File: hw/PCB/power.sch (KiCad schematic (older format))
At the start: 12 parts, among them J4 Battery, U0 AP7215-33YG-13, U3 AV4524

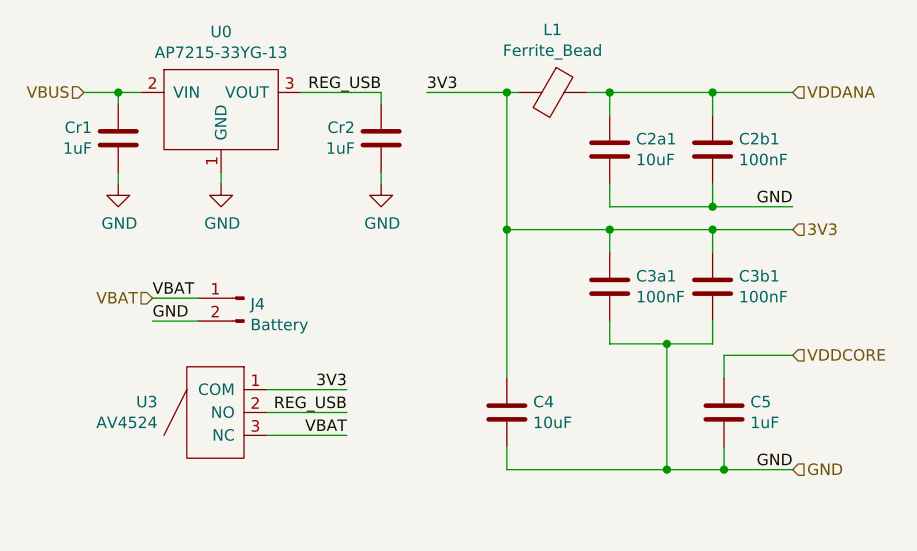
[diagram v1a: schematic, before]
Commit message: Added a footprint library for a micro SD card. Updated the schematic. Replaced the SAMD21G with the SAMD21E (32 pin variant). Added a data logger and a reset button.
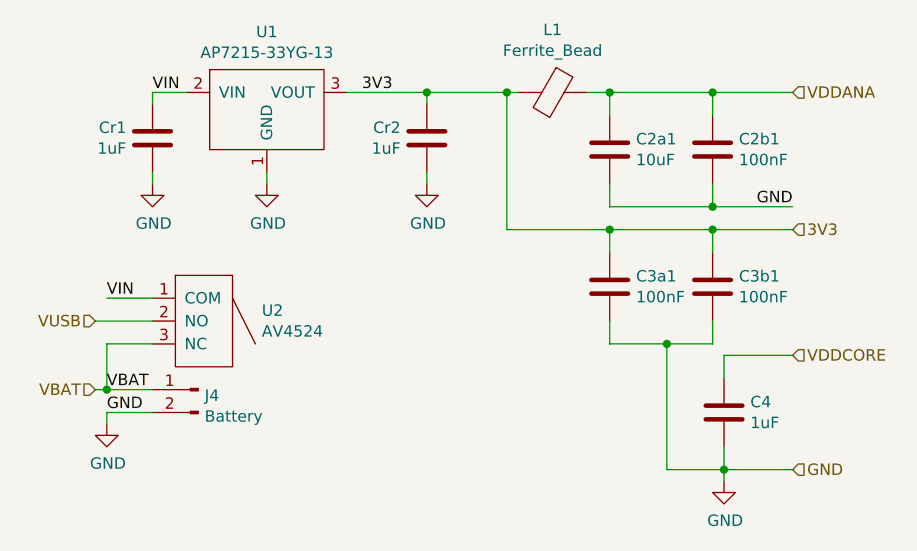
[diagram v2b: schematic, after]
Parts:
- removed C4: 10uF, Capacitor_SMD:C_0603_1608Metric_Pad1.05x0.95mm_HandSolder, symbol Device:C
- removed U3: AV4524, Interrupt:AV4524, symbol Interrupter:AV4524
- added U2: AV4524, Interrupt:AV4524, symbol Interrupter:AV4524
- renumbered C5 to C4, U0 to U1
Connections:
- net REG_USB is gone; now on net 3V3: Cr2.1, U1.3 (VOUT)
- net VBAT: now also U2.3 (NC)
- net VBUS renamed VIN
- net VIN: now also U2.1 (COM)
- new net VUSB: U2.2 (NO)
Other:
- moved on the sheet: Cr1, Cr2, J4, U1
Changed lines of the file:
@@
 $EndComp
 $Comp
-L Device:C C5
+L Device:C C4
 U 1 1 5B635301
 P 5100 4800
-F 0 "C5" H 5215 4846 50  0000 L CNN
+F 0 "C4" H 5215 4846 50  0000 L CNN
 F 1 "1uF" H 5215 4755 50  0000 L CNN
 F 2 "Capacitor_SMD:C_0603_1608Metric_Pad1.05x0.95mm_HandSolder" H 5138 4650 50  0001 C CNN
@@
 $EndComp
 $Comp
-L Device:C C4
-U 1 1 5B635382
-P 4150 4800
-F 0 "C4" H 4265 4846 50  0000 L CNN
-F 1 "10uF" H 4265 4755 50  0000 L CNN
-F 2 "Capacitor_SMD:C_0603_1608Metric_Pad1.05x0.95mm_HandSolder" H 4188 4650 50  0001 C CNN
-F 3 "~" H 4150 4800 50  0001 C CNN
-	1    4150 4800
-	1    0    0    -1
-$EndComp
-$Comp
 L Device:C C3a1
 U 1 1 5B6353CA
@@
 Text HLabel 5400 5050 2    50   Input ~ 0
 GND
-Wire Wire Line
-	4150 4650 4150 4000
-Wire Wire Line
-	4150 4950 4150 5050
-Wire Wire Line
-	4150 5050 4850 5050
 Connection ~ 5100 5050
 Text Label 5400 3900 2    50   ~ 0
 GND
-Text Label 5400 5050 2    50   ~ 0
+Text Label 2400 4800 0    50   ~ 0
 GND
-Connection ~ 4150 4000
 Wire Wire Line
 	4150 4000 4150 3400
@@
 Wire Wire Line
 	4850 4500 4600 4500
-Connection ~ 4850 5050
 Wire Wire Line
 	4850 5050 5100 5050
@@
 Connection ~ 4850 4500
 $Comp
-L power_regul:AP7215-33YG-13 U0
+L power_regul:AP7215-33YG-13 U1
 U 1 1 5BB07412
-P 2900 3550
-F 0 "U0" H 2900 3965 50  0000 C CNN
-F 1 "AP7215-33YG-13" H 2900 3874 50  0000 C CNN
-F 2 "Package_TO_SOT_SMD:SOT-89-3_Handsoldering" H 2900 3550 50  0001 C CNN
-F 3 "" H 2900 3550 50  0001 C CNN
-	1    2900 3550
+P 3100 3550
+F 0 "U1" H 3100 3965 50  0000 C CNN
+F 1 "AP7215-33YG-13" H 3100 3874 50  0000 C CNN
+F 2 "Package_TO_SOT_SMD:SOT-89-3_Handsoldering" H 3100 3550 50  0001 C CNN
+F 3 "" H 3100 3550 50  0001 C CNN
+	1    3100 3550
 	1    0    0    -1
 $EndComp
@@
 	5400 4000 5050 4000
 Connection ~ 5050 4000
-Text HLabel 2300 3400 0    50   Input ~ 0
-VBUS
 $Comp
 L Device:C Cr1
 U 1 1 5BB30701
-P 2450 3600
-F 0 "Cr1" H 2565 3646 50  0000 L CNN
-F 1 "1uF" H 2565 3555 50  0000 L CNN
-F 2 "Capacitor_SMD:C_0603_1608Metric_Pad1.05x0.95mm_HandSolder" H 2488 3450 50  0001 C CNN
-F 3 "~" H 2450 3600 50  0001 C CNN
-	1    2450 3600
+P 2600 3600
+F 0 "Cr1" H 2715 3646 50  0000 L CNN
+F 1 "1uF" H 2715 3555 50  0000 L CNN
+F 2 "Capacitor_SMD:C_0603_1608Metric_Pad1.05x0.95mm_HandSolder" H 2638 3450 50  0001 C CNN
+F 3 "~" H 2600 3600 50  0001 C CNN
+	1    2600 3600
 	-1   0    0    -1
 $EndComp
@@
 L Device:C Cr2
 U 1 1 5BB3073D
-P 3600 3600
-F 0 "Cr2" H 3715 3646 50  0000 L CNN
-F 1 "1uF" H 3715 3555 50  0000 L CNN
-F 2 "Capacitor_SMD:C_0603_1608Metric_Pad1.05x0.95mm_HandSolder" H 3638 3450 50  0001 C CNN
-F 3 "~" H 3600 3600 50  0001 C CNN
-	1    3600 3600
+P 3800 3600
+F 0 "Cr2" H 3915 3646 50  0000 L CNN
+F 1 "1uF" H 3915 3555 50  0000 L CNN
+F 2 "Capacitor_SMD:C_0603_1608Metric_Pad1.05x0.95mm_HandSolder" H 3838 3450 50  0001 C CNN
+F 3 "~" H 3800 3600 50  0001 C CNN
+	1    3800 3600
 	-1   0    0    -1
 $EndComp
 Connection ~ 4150 3400
 Wire Wire Line
-	2300 3400 2450 3400
-Wire Wire Line
-	2450 3450 2450 3400
-Connection ~ 2450 3400
-Wire Wire Line
-	2450 3400 2550 3400
-Wire Wire Line
-	2450 3750 2450 3800
-Wire Wire Line
-	3600 3750 3600 3800
+	2600 3450 2600 3400
+Wire Wire Line
+	2600 3750 2600 3800
+Wire Wire Line
+	3800 3750 3800 3800
 $Comp
 L power:GND #PWR0107
 U 1 1 5BB332C0
-P 2450 3800
-F 0 "#PWR0107" H 2450 3550 50  0001 C CNN
-F 1 "GND" H 2455 3627 50  0000 C CNN
-F 2 "" H 2450 3800 50  0001 C CNN
-F 3 "" H 2450 3800 50  0001 C CNN
-	1    2450 3800
+P 2600 3800
+F 0 "#PWR0107" H 2600 3550 50  0001 C CNN
+F 1 "GND" H 2605 3627 50  0000 C CNN
+F 2 "" H 2600 3800 50  0001 C CNN
+F 3 "" H 2600 3800 50  0001 C CNN
+	1    2600 3800
 	1    0    0    -1
 $EndComp
@@
 L power:GND #PWR0108
 U 1 1 5BB332E6
-P 3600 3800
-F 0 "#PWR0108" H 3600 3550 50  0001 C CNN
-F 1 "GND" H 3605 3627 50  0000 C CNN
-F 2 "" H 3600 3800 50  0001 C CNN
-F 3 "" H 3600 3800 50  0001 C CNN
-	1    3600 3800
+P 3800 3800
+F 0 "#PWR0108" H 3800 3550 50  0001 C CNN
+F 1 "GND" H 3805 3627 50  0000 C CNN
+F 2 "" H 3800 3800 50  0001 C CNN
+F 3 "" H 3800 3800 50  0001 C CNN
+	1    3800 3800
 	1    0    0    -1
 $EndComp
@@
 L power:GND #PWR0113
 U 1 1 5BF7FABB
-P 2900 3800
-F 0 "#PWR0113" H 2900 3550 50  0001 C CNN
-F 1 "GND" H 2905 3627 50  0000 C CNN
-F 2 "" H 2900 3800 50  0001 C CNN
-F 3 "" H 2900 3800 50  0001 C CNN
-	1    2900 3800
-	1    0    0    -1
-$EndComp
-Wire Wire Line
-	2900 3800 2900 3750
-Text Label 3600 3400 2    50   ~ 0
-REG_USB
-Wire Wire Line
-	3250 3400 3600 3400
-Text Label 3800 3400 0    50   ~ 0
+P 3100 3800
+F 0 "#PWR0113" H 3100 3550 50  0001 C CNN
+F 1 "GND" H 3105 3627 50  0000 C CNN
+F 2 "" H 3100 3800 50  0001 C CNN
+F 3 "" H 3100 3800 50  0001 C CNN
+	1    3100 3800
+	1    0    0    -1
+$EndComp
+Wire Wire Line
+	3100 3800 3100 3750
+Wire Wire Line
+	3450 3400 3800 3400
+Text Label 3650 3400 2    50   ~ 0
 3V3
-Text HLabel 2600 4300 0    50   Input ~ 0
-VBAT
 $Comp
 L Connector:Conn_01x02_Male J4
 U 1 1 5BFD4B3E
-P 3000 4300
-F 0 "J4" H 2972 4274 50  0000 R CNN
-F 1 "Battery" H 2972 4183 50  0000 R CNN
-F 2 "Connector_JST:JST_PH_S2B-PH-K_1x02_P2.00mm_Horizontal" H 3000 4300 50  0001 C CNN
-F 3 "~" H 3000 4300 50  0001 C CNN
-	1    3000 4300
+P 2800 4700
+F 0 "J4" H 2772 4674 50  0000 R CNN
+F 1 "Battery" H 2772 4583 50  0000 R CNN
+F 2 "Connector_JST:JST_PH_S2B-PH-K_1x02_P2.00mm_Horizontal" H 2800 4700 50  0001 C CNN
+F 3 "~" H 2800 4700 50  0001 C CNN
+	1    2800 4700
 	-1   0    0    -1
 $EndComp
-Text Label 2600 4400 0    50   ~ 0
-GND
-Text Label 2600 4300 0    50   ~ 0
+Wire Wire Line
+	3800 3400 4150 3400
+Wire Wire Line
+	3800 3450 3800 3400
+$Comp
+L Interrupter:AV4524 U2
+U 1 1 5D1D3759
+P 2800 4400
+F 0 "U2" H 3078 4446 50  0000 L CNN
+F 1 "AV4524" H 3078 4355 50  0000 L CNN
+F 2 "Interrupt:AV4524" H 2750 4400 50  0001 C CNN
+F 3 "" H 2750 4400 50  0001 C CNN
+	1    2800 4400
+	1    0    0    -1
+$EndComp
+Text HLabel 2350 4700 0    50   Input ~ 0
 VBAT
-Wire Wire Line
-	2800 4300 2600 4300
-Wire Wire Line
-	2600 4400 2800 4400
-Wire Wire Line
-	3800 3400 4150 3400
-Wire Wire Line
-	3600 3450 3600 3400
-$Comp
-L Interrupter:AV4524 U3
-U 1 1 5BFC5BF6
-P 2900 4800
-F 0 "U3" H 3178 4846 50  0000 L CNN
-F 1 "AV4524" H 3178 4755 50  0000 L CNN
-F 2 "Interrupt:AV4524" H 2850 4800 50  0001 C CNN
-F 3 "" H 2850 4800 50  0001 C CNN
-	1    2900 4800
-	-1   0    0    -1
-$EndComp
-Text Label 3450 4700 2    50   ~ 0
-3V3
-Text Label 3450 4900 2    50   ~ 0
+Text HLabel 2350 4400 0    50   Input ~ 0
+VUSB
+Text Label 2400 4300 0    50   ~ 0
+VIN
+Text Label 2400 4700 0    50   ~ 0
 VBAT
-Text Label 3450 4800 2    50   ~ 0
-REG_USB
-Wire Wire Line
-	3450 4800 3100 4800
-Wire Wire Line
-	3100 4900 3450 4900
-Wire Wire Line
-	3100 4700 3450 4700
+Wire Wire Line
+	2600 4400 2350 4400
+Wire Wire Line
+	2600 4500 2400 4500
+Wire Wire Line
+	2600 4300 2400 4300
+Wire Wire Line
+	2400 4500 2400 4700
+Wire Wire Line
+	2400 4700 2600 4700
+$Comp
+L power:GND #PWR?
+U 1 1 5D1DFE0F
+P 2400 4850
+F 0 "#PWR?" H 2400 4600 50  0001 C CNN
+F 1 "GND" H 2405 4677 50  0000 C CNN
+F 2 "" H 2400 4850 50  0001 C CNN
+F 3 "" H 2400 4850 50  0001 C CNN
+	1    2400 4850
+	1    0    0    -1
+$EndComp
+Text Label 2600 3400 0    50   ~ 0
+VIN
+Connection ~ 3800 3400
+Wire Wire Line
+	2400 4800 2600 4800
+Wire Wire Line
+	2400 4850 2400 4800
+$Comp
+L power:GND #PWR?
+U 1 1 5D1EBCCE
+P 5100 5100
+F 0 "#PWR?" H 5100 4850 50  0001 C CNN
+F 1 "GND" H 5105 4927 50  0000 C CNN
+F 2 "" H 5100 5100 50  0001 C CNN
+F 3 "" H 5100 5100 50  0001 C CNN
+	1    5100 5100
+	1    0    0    -1
+$EndComp
+Wire Wire Line
+	5100 5100 5100 5050
+Wire Wire Line
+	2600 3400 2750 3400
+Wire Wire Line
+	2400 4700 2350 4700
+Connection ~ 2400 4700
 $EndSCHEMATC

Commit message: Started the new design of the PCB's layout.
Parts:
- U1: footprint Package_TO_SOT_SMD:SOT-89-3_Handsoldering -> Package_TO_SOT_SMD:SOT-89-3
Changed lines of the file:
@@
 $Descr A4 11693 8268
 encoding utf-8
-Sheet 2 5
+Sheet 2 6
 Title ""
 Date ""
@@
 F 0 "U1" H 3100 3965 50  0000 C CNN
 F 1 "AP7215-33YG-13" H 3100 3874 50  0000 C CNN
-F 2 "Package_TO_SOT_SMD:SOT-89-3_Handsoldering" H 3100 3550 50  0001 C CNN
+F 2 "Package_TO_SOT_SMD:SOT-89-3" H 3100 3550 50  0001 C CNN
 F 3 "" H 3100 3550 50  0001 C CNN
 	1    3100 3550
@@
 	2400 4700 2600 4700
 $Comp
-L power:GND #PWR?
+L power:GND #PWR0115
 U 1 1 5D1DFE0F
 P 2400 4850
-F 0 "#PWR?" H 2400 4600 50  0001 C CNN
+F 0 "#PWR0115" H 2400 4600 50  0001 C CNN
 F 1 "GND" H 2405 4677 50  0000 C CNN
 F 2 "" H 2400 4850 50  0001 C CNN
@@
 	2400 4850 2400 4800
 $Comp
-L power:GND #PWR?
+L power:GND #PWR0116
 U 1 1 5D1EBCCE
 P 5100 5100
-F 0 "#PWR?" H 5100 4850 50  0001 C CNN
+F 0 "#PWR0116" H 5100 4850 50  0001 C CNN
 F 1 "GND" H 5105 4927 50  0000 C CNN
 F 2 "" H 5100 5100 50  0001 C CNN

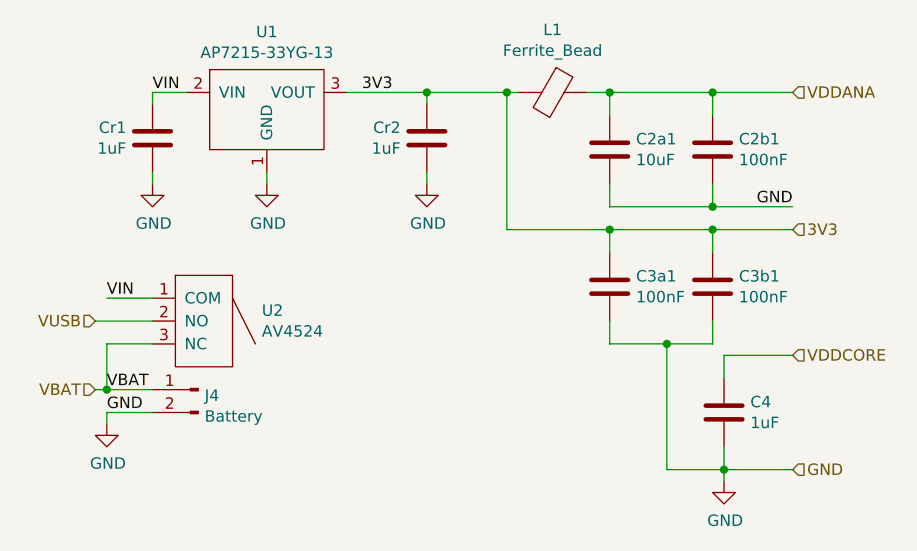
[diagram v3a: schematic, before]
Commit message: Replaced a 100nF capacitor with a 10uF capacitor. Worked on PCB preliminary layout.
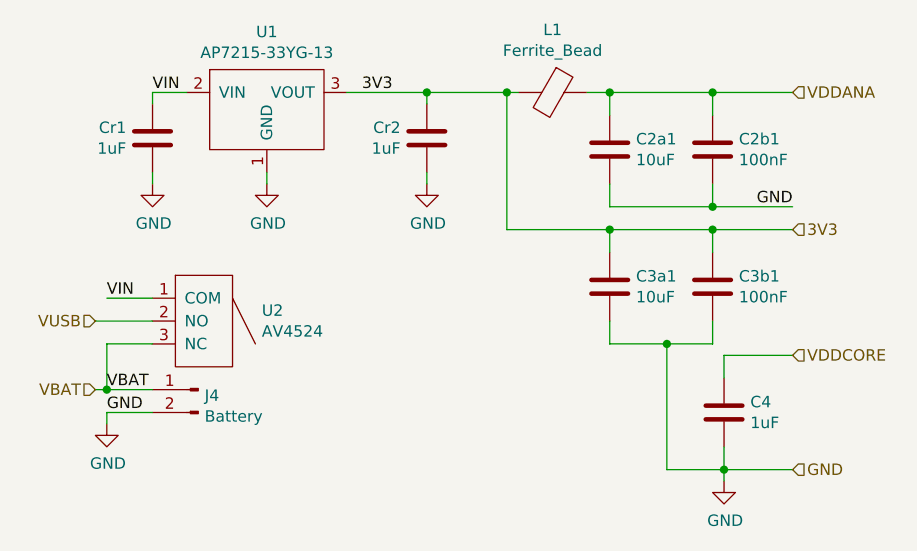
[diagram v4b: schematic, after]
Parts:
- C3a1: value 100nF -> 10uF
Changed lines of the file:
@@
 P 4600 4250
 F 0 "C3a1" H 4715 4296 50  0000 L CNN
-F 1 "100nF" H 4715 4205 50  0000 L CNN
+F 1 "10uF" H 4715 4205 50  0000 L CNN
 F 2 "Capacitor_SMD:C_0603_1608Metric_Pad1.05x0.95mm_HandSolder" H 4638 4100 50  0001 C CNN
 F 3 "~" H 4600 4250 50  0001 C CNN
